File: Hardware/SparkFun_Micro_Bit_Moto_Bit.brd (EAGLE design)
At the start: 76.2 x 58.4 mm, 38 parts, among them J1 5.5x2.1mm Barrel, J2 CORTEX_DEBUGPTH, U1 CY8C4245LQI-483, U2 TPS62172, U3 micro:bit, U4 DRV8835

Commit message: Changed name from motobit to follow naming conventions
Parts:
- added D1: RED, SparkFun-LED:LED-0603
- added R3, R4: 4.7k, SparkFun-Resistors:0603
- added R5: 470, SparkFun-Resistors:0603
- U$1: device SparkFun-Hardware:STAND-OFF -> SparkFun-Aesthetics:PRODUCTION_INSTRUCTIONS
- moved U$1 82.9 mm to (-7.62, -33.0)
- moved LOGO2 14.2 mm to (15.2, 12.7)
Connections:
- new net N$6: R3.1, U1.18
- new net N$7: R4.1, U1.19
- new net N$8: D1.A, R5.2
- new net SLED: R5.1, U1.14
- net 3.3V: now also R3.2, R4.2
- net GND: now also D1.C
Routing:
- net P3.3: track 13.5 -> 18.8 mm, vias 0 -> 1
- net 3.3V: track 197.0 -> 201.8 mm, vias 1 -> 2
- net N$6: track 0.00 -> 3.71 mm
- net SLED: track 0.00 -> 3.51 mm
- net N$7: track 0.00 -> 3.28 mm
- net N$8: track 0.00 -> 1.55 mm
- net P3.2: track 14.9 -> 14.0 mm, vias 0 -> 1
- net GND: vias 27 -> 28
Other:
- board text added: "- Solder mask color : Black"
- board text added: "STAT"
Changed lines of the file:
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@@
 <layer number="37" name="tTest" color="7" fill="1" visible="no" active="yes"/>
 <layer number="38" name="bTest" color="7" fill="1" visible="no" active="yes"/>
-<layer number="39" name="tKeepout" color="4" fill="11" visible="no" active="yes"/>
-<layer number="40" name="bKeepout" color="1" fill="11" visible="no" active="yes"/>
+<layer number="39" name="tKeepout" color="4" fill="11" visible="yes" active="yes"/>
+<layer number="40" name="bKeepout" color="1" fill="11" visible="yes" active="yes"/>
 <layer number="41" name="tRestrict" color="4" fill="10" visible="no" active="yes"/>
 <layer number="42" name="bRestrict" color="1" fill="10" visible="no" active="yes"/>
@@
 <layer number="45" name="Holes" color="7" fill="1" visible="no" active="yes"/>
 <layer number="46" name="Milling" color="3" fill="1" visible="no" active="yes"/>
-<layer number="47" name="Measures" color="7" fill="1" visible="yes" active="yes"/>
+<layer number="47" name="Measures" color="7" fill="1" visible="no" active="yes"/>
 <layer number="48" name="Document" color="7" fill="1" visible="no" active="yes"/>
 <layer number="49" name="Reference" color="7" fill="1" visible="no" active="yes"/>
@@
 <text x="39.37" y="3.81" size="1.27" layer="22" font="vector" ratio="15" rot="MR180" align="bottom-center">0x59</text>
 <text x="62.23" y="0.508" size="1.27" layer="16" font="vector" ratio="15" rot="MR0" align="bottom-center">v01</text>
+<text x="26.67" y="27.813" size="1.016" layer="21" font="vector" ratio="15">STAT</text>
+<text x="-5.08" y="-45.72" size="1.27" layer="51" font="vector" ratio="15">- Solder mask color : Black</text>
 </plain>
 <attributes>
@@
 <attribute name="PROD_ID" value="CAP-08402" x="31.242" y="32.0167" size="1.778" layer="27" font="vector" ratio="15" rot="R90" display="off"/>
 </element>
-<element name="U$1" library="SparkFun-Hardware" package="STAND-OFF" value="" x="45.72" y="30.48"/>
 <element name="LOGO1" library="SparkFun-Aesthetics" package="SFE_LOGO_NAME_FLAME_.2" value="SFE_LOGO_NAME_FLAME.2_INCH" x="1.27" y="19.05"/>
-<element name="LOGO2" library="SparkFun-Aesthetics" package="OSHW-LOGO-M" value="OSHW-LOGOM" x="27.94" y="19.05"/>
+<element name="LOGO2" library="SparkFun-Aesthetics" package="OSHW-LOGO-M" value="OSHW-LOGOM" x="15.24" y="12.7"/>
 <element name="FD1" library="SparkFun-Aesthetics" package="FIDUCIAL-MICRO" value="FIDUCIALUFIDUCIAL" x="58.039" y="1.397"/>
 <element name="FD2" library="SparkFun-Aesthetics" package="FIDUCIAL-MICRO" value="FIDUCIALUFIDUCIAL" x="1.27" y="57.15"/>
@@
 <element name="TP3" library="SparkFun-Connectors" package="PAD.03X.03" value="" x="26.67" y="19.05" rot="MR0"/>
 <element name="TP4" library="SparkFun-Connectors" package="PAD.03X.03" value="" x="24.13" y="19.05" rot="MR0"/>
+<element name="R3" library="SparkFun-Resistors" package="0603" value="4.7k" x="28.448" y="23.495" rot="R180">
+<attribute name="PROD_ID" value="RES-07857" x="28.448" y="23.495" size="1.778" layer="27" ratio="15" rot="R180" display="off"/>
+</element>
+<element name="R4" library="SparkFun-Resistors" package="0603" value="4.7k" x="28.448" y="21.971" rot="R180">
+<attribute name="PROD_ID" value="RES-07857" x="28.448" y="21.971" size="1.778" layer="27" ratio="15" rot="R180" display="off"/>
+</element>
+<element name="D1" library="SparkFun-LED" package="LED-0603" value="RED" x="28.448" y="26.543">
+<attribute name="PROD_ID" value="DIO-00819" x="28.448" y="26.543" size="1.778" layer="27" ratio="15" display="off"/>
+</element>
+<element name="R5" library="SparkFun-Resistors" package="0603" value="470" x="28.448" y="25.019" rot="R180">
+<attribute name="PROD_ID" value="RES-07869" x="28.448" y="25.019" size="1.778" layer="27" ratio="15" rot="R180" display="off"/>
+</element>
+<element name="U$1" library="SparkFun-Aesthetics" package="PRODUCTION_INSTRUCTIONS" value="" x="-7.62" y="-33.02"/>
 </elements>
 <signals>
@@
 <wire x1="33.5814" y1="27.051" x2="33.02" y2="27.051" width="0.2032" layer="1"/>
 <contactref element="TP4" pad="P$1"/>
+<via x="45.72" y="30.48" extent="1-16" drill="3.302"/>
+<contactref element="D1" pad="C"/>
 </signal>
 <signal name="3.3V">
@@
 <wire x1="26.67" y1="16.637" x2="29.21" y2="14.097" width="0.6096" layer="16"/>
 <wire x1="29.21" y1="14.097" x2="30.226" y2="14.097" width="0.6096" layer="16"/>
+<contactref element="R4" pad="2"/>
+<contactref element="R3" pad="2"/>
+<wire x1="26.67" y1="19.05" x2="26.67" y2="19.392" width="0.6096" layer="16"/>
+<wire x1="26.67" y1="19.392" x2="27.598" y2="20.32" width="0.6096" layer="16"/>
+<via x="27.598" y="20.32" extent="1-16" drill="0.381"/>
+<wire x1="27.598" y1="20.32" x2="27.598" y2="21.971" width="0.6096" layer="1"/>
+<wire x1="27.598" y1="21.971" x2="27.598" y2="23.495" width="0.6096" layer="1"/>
 </signal>
 <signal name="SDA">
@@
 <contactref element="U1" pad="12"/>
 <contactref element="J2" pad="2"/>
-<wire x1="30.226" y1="15.367" x2="30.226" y2="17.907" width="0.2032" layer="1"/>
-<wire x1="30.226" y1="17.907" x2="30.861" y2="18.542" width="0.2032" layer="1"/>
-<wire x1="30.861" y1="18.542" x2="30.861" y2="24.067996875" width="0.2032" layer="1"/>
-<wire x1="30.861" y1="24.067996875" x2="31.657003125" y2="24.864" width="0.2032" layer="1"/>
-<wire x1="31.657003125" y1="24.864" x2="32.3314" y2="24.864" width="0.2032" layer="1"/>
 <contactref element="TP1" pad="P$1"/>
-<wire x1="29.21" y1="19.05" x2="30.226" y2="18.034" width="0.254" layer="16"/>
-<wire x1="30.226" y1="18.034" x2="30.226" y2="15.367" width="0.254" layer="16"/>
+<wire x1="32.3314" y1="24.864" x2="31.823384375" y2="24.864" width="0.254" layer="1"/>
+<wire x1="31.823384375" y1="24.864" x2="31.623" y2="25.064384375" width="0.254" layer="1"/>
+<wire x1="31.623" y1="25.064384375" x2="31.623" y2="26.035" width="0.254" layer="1"/>
+<via x="31.623" y="26.035" extent="1-16" drill="0.381"/>
+<wire x1="30.226" y1="15.367" x2="30.226" y2="19.05" width="0.254" layer="16"/>
+<wire x1="30.226" y1="19.05" x2="30.226" y2="24.638" width="0.254" layer="16"/>
+<wire x1="30.226" y1="24.638" x2="31.623" y2="26.035" width="0.254" layer="16"/>
+<wire x1="29.21" y1="19.05" x2="30.226" y2="19.05" width="0.254" layer="16"/>
 </signal>
 <signal name="P3.3">
 <contactref element="U1" pad="13"/>
 <contactref element="J2" pad="4"/>
-<wire x1="31.496" y1="15.367" x2="31.496" y2="17.907" width="0.2032" layer="1"/>
-<wire x1="31.496" y1="17.907" x2="31.369" y2="18.034" width="0.2032" layer="1"/>
-<wire x1="31.369" y1="18.034" x2="31.369" y2="23.91688125" width="0.2032" layer="1"/>
-<wire x1="31.369" y1="23.91688125" x2="31.81611875" y2="24.364" width="0.2032" layer="1"/>
-<wire x1="31.81611875" y1="24.364" x2="32.3314" y2="24.364" width="0.2032" layer="1"/>
 <contactref element="TP2" pad="P$1"/>
-<wire x1="31.75" y1="19.05" x2="31.496" y2="18.796" width="0.254" layer="16"/>
-<wire x1="31.496" y1="18.796" x2="31.496" y2="15.367" width="0.254" layer="16"/>
+<wire x1="32.3314" y1="24.364" x2="31.466696875" y2="24.364" width="0.254" layer="1"/>
+<wire x1="31.466696875" y1="24.364" x2="30.734" y2="25.096696875" width="0.254" layer="1"/>
+<wire x1="30.734" y1="25.096696875" x2="30.734" y2="26.797" width="0.254" layer="1"/>
+<via x="31.242" y="27.305" extent="1-16" drill="0.381"/>
+<wire x1="30.734" y1="26.797" x2="31.242" y2="27.305" width="0.254" layer="1"/>
+<wire x1="31.75" y1="19.05" x2="30.861" y2="19.05" width="0.254" layer="16"/>
+<wire x1="30.861" y1="19.05" x2="30.861" y2="24.13" width="0.254" layer="16"/>
+<wire x1="30.861" y1="24.13" x2="32.385" y2="25.654" width="0.254" layer="16"/>
+<wire x1="32.385" y1="25.654" x2="32.385" y2="26.67" width="0.254" layer="16"/>
+<wire x1="32.385" y1="26.67" x2="31.75" y2="27.305" width="0.254" layer="16"/>
+<wire x1="31.75" y1="27.305" x2="31.242" y2="27.305" width="0.254" layer="16"/>
+<wire x1="31.496" y1="15.367" x2="30.861" y2="16.002" width="0.254" layer="16"/>
+<wire x1="30.861" y1="16.002" x2="30.861" y2="19.05" width="0.254" layer="16"/>
 </signal>
 <signal name="P0.4">
@@
 <wire x1="34.5814" y1="19.30425" x2="34.5814" y2="20.114" width="0.254" layer="1"/>
 </signal>
+<signal name="N$6">
+<contactref element="U1" pad="18"/>
+<contactref element="R3" pad="1"/>
+<wire x1="29.298" y1="23.495" x2="30.033740625" y2="23.495" width="0.254" layer="1"/>
+<wire x1="31.664740625" y1="21.864" x2="32.3314" y2="21.864" width="0.254" layer="1"/>
+<wire x1="31.664740625" y1="21.864" x2="30.033740625" y2="23.495" width="0.254" layer="1"/>
+</signal>
+<signal name="N$7">
+<contactref element="U1" pad="19"/>
+<contactref element="R4" pad="1"/>
+<wire x1="29.298" y1="21.971" x2="30.127" y2="21.971" width="0.254" layer="1"/>
+<wire x1="30.734" y1="21.364" x2="32.3314" y2="21.364" width="0.254" layer="1"/>
+<wire x1="30.734" y1="21.364" x2="30.127" y2="21.971" width="0.254" layer="1"/>
+</signal>
+<signal name="SLED">
+<contactref element="U1" pad="14"/>
+<contactref element="R5" pad="1"/>
+<wire x1="29.298" y1="25.019" x2="30.0134625" y2="25.019" width="0.254" layer="1"/>
+<wire x1="31.1684625" y1="23.864" x2="32.3314" y2="23.864" width="0.254" layer="1"/>
+<wire x1="31.1684625" y1="23.864" x2="30.0134625" y2="25.019" width="0.254" layer="1"/>
+</signal>
+<signal name="N$8">
+<contactref element="R5" pad="2"/>
+<contactref element="D1" pad="A"/>
+<wire x1="27.571" y1="26.543" x2="27.571" y2="25.019" width="0.254" layer="1"/>
+<wire x1="27.571" y1="25.019" x2="27.598" y2="25.019" width="0.254" layer="1"/>
+</signal>
 </signals>

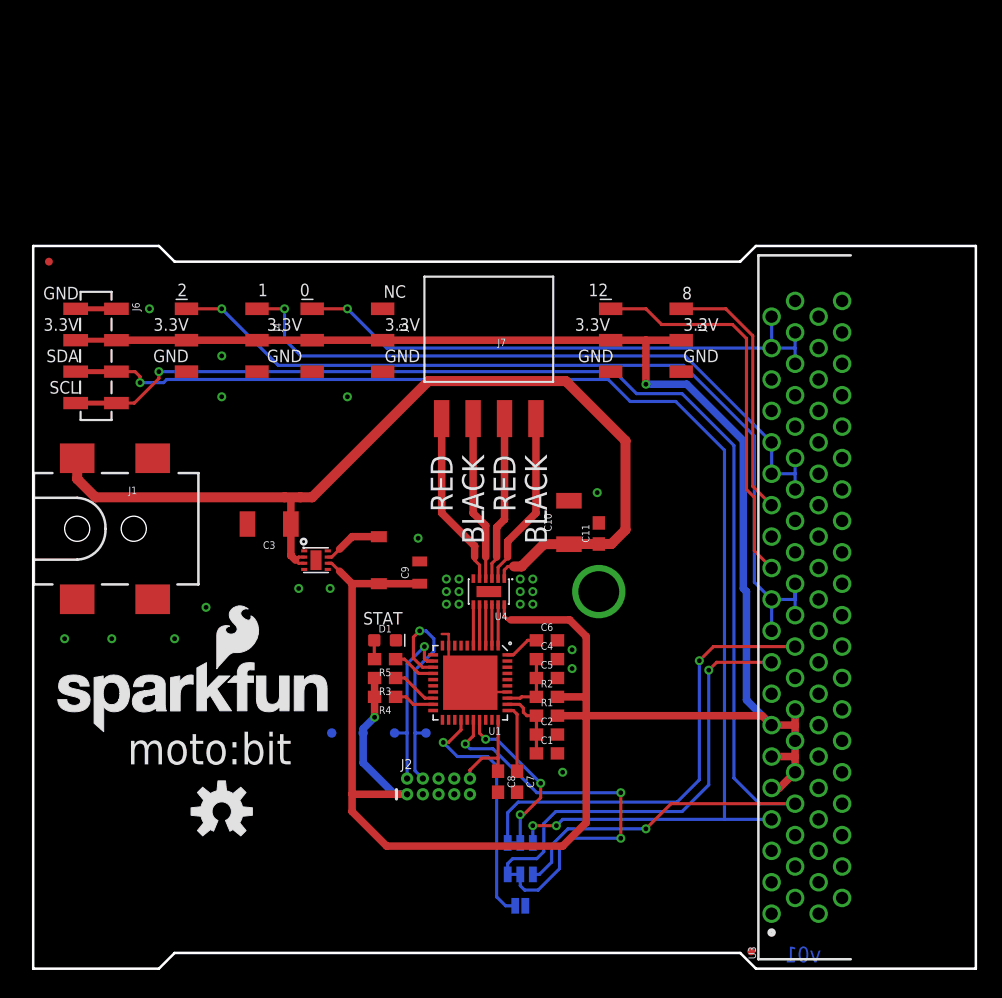
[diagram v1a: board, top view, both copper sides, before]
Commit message: Design Review Changes
- Added staking vias to barrel connector and motor connector
- Added two servo connectors
- Moved vias that were exposed for motor driver heatsink
- Added selective solder path
- Added mounting holes
- Rounded corners to match micro:bit
- Rotated silk to match micro:bit silk orientation
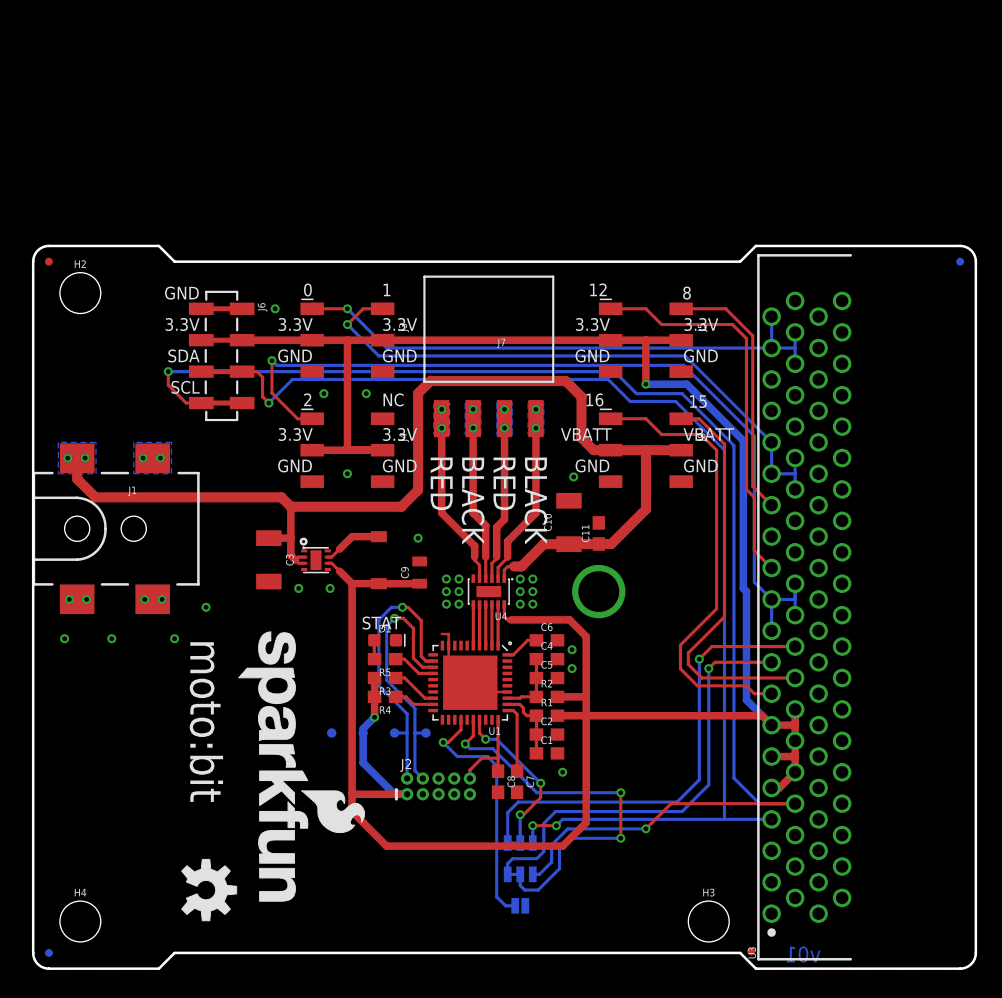
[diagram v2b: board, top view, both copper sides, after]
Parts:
- added FD3, FD4: FIDUCIALUFIDUCIAL, SparkFun-Aesthetics:FIDUCIAL-MICRO
- added H2, H3, H4: STAND-OFF, SparkFun-Hardware:STAND-OFF
- added J8: (no value), SparkFun-Connectors:2X3_SMD
- J6: value (none) -> 1X04_SMD_STRAIGHT_COMBO
- L1: value 4.7µH -> 2.2µH
- moved LOGO1 17.6 mm to (16.5, 27.9), turned to 270 degrees
- moved J4 13.5 mm to (25.4, 41.9)
- moved J6 10.2 mm to (15.2, 53.3)
- moved LOGO2 6.48 mm to (14.0, 6.35), turned to 270 degrees
- moved C3 2.90 mm to (19.1, 33.0), turned to 270 degrees
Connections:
- removed net BIN1: U3.A16
- removed net BIN2: U3.A15
- new net SERVO_15: J8.2, U3.A16
- new net SERVO_16: J8.1, U3.A15
- net ANALOG_1: now also J3.2; no longer J4.2
- net GND: now also J8.5, J8.6
- net V_BATT: now also J8.3, J8.4
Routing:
- net SERVO_16: track 0.00 -> 36.7 mm
- net SERVO_15: track 0.00 -> 32.5 mm
- net V_BATT: track 79.7 -> 93.4 mm, vias 0 -> 2
- net P3.2: track 14.0 -> 23.1 mm
- net SDA: track 106.3 -> 98.2 mm
- net 3.3V: track 201.8 -> 209.1 mm
- net ANALOG_1: track 54.5 -> 48.6 mm
- net P3.3: track 18.8 -> 21.5 mm
- net SCL: track 110.8 -> 112.9 mm
- net ANALOG_2: track 72.2 -> 70.3 mm
- net N$5: track 0.00 -> 1.40 mm, vias 0 -> 2
- net BO2: track 14.2 -> 14.9 mm, vias 0 -> 2
- net BO1: track 13.4 -> 14.1 mm, vias 0 -> 2
- net AO2: track 13.4 -> 14.1 mm, vias 0 -> 2
- net AO1: track 14.2 -> 14.9 mm, vias 0 -> 2
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- added copper zone on layer 16, net AO1
- added copper zone on layer 16, net AO2
- added copper zone on layer 16, net BO1
- added copper zone on layer 16, net BO2
- added copper zone on layer 16, net N$5
- added copper zone on layer 16, net V_BATT
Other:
- outline, holes or cut-outs redrawn
- board text added: "15"
- board text added: "16"
- board text added: "VBATT"

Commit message: QC Fixes
- Removed excess copper around PSoC center pad
- Added names and values to buck converter and inductor
- Added note about solder mask color finish
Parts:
- L1: value 2.2µH -> 2.2µH/±20%/1.5A
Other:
- board text added: "- Solder mask color : Black (Gloss if available)"
- board text removed: "- Solder mask color : Black"
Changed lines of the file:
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@@
 <layer number="20" name="Dimension" color="15" fill="1" visible="yes" active="yes"/>
 <layer number="21" name="tPlace" color="16" fill="1" visible="yes" active="yes"/>
-<layer number="22" name="bPlace" color="14" fill="1" visible="no" active="yes"/>
+<layer number="22" name="bPlace" color="14" fill="1" visible="yes" active="yes"/>
 <layer number="23" name="tOrigins" color="15" fill="1" visible="yes" active="yes"/>
-<layer number="24" name="bOrigins" color="15" fill="1" visible="no" active="yes"/>
+<layer number="24" name="bOrigins" color="15" fill="1" visible="yes" active="yes"/>
 <layer number="25" name="tNames" color="7" fill="1" visible="no" active="yes"/>
 <layer number="26" name="bNames" color="7" fill="1" visible="no" active="yes"/>
 <layer number="27" name="tValues" color="7" fill="1" visible="no" active="yes"/>
 <layer number="28" name="bValues" color="7" fill="1" visible="no" active="yes"/>
-<layer number="29" name="tStop" color="7" fill="3" visible="no" active="yes"/>
-<layer number="30" name="bStop" color="7" fill="6" visible="no" active="yes"/>
+<layer number="29" name="tStop" color="7" fill="3" visible="yes" active="yes"/>
+<layer number="30" name="bStop" color="7" fill="6" visible="yes" active="yes"/>
 <layer number="31" name="tCream" color="7" fill="4" visible="no" active="yes"/>
 <layer number="32" name="bCream" color="7" fill="5" visible="no" active="yes"/>
@@
 <layer number="38" name="bTest" color="7" fill="1" visible="no" active="yes"/>
 <layer number="39" name="tKeepout" color="4" fill="11" visible="yes" active="yes"/>
-<layer number="40" name="bKeepout" color="1" fill="11" visible="yes" active="yes"/>
+<layer number="40" name="bKeepout" color="1" fill="11" visible="no" active="yes"/>
 <layer number="41" name="tRestrict" color="4" fill="10" visible="no" active="yes"/>
 <layer number="42" name="bRestrict" color="1" fill="10" visible="no" active="yes"/>
 <layer number="43" name="vRestrict" color="2" fill="10" visible="no" active="yes"/>
 <layer number="44" name="Drills" color="7" fill="1" visible="no" active="yes"/>
-<layer number="45" name="Holes" color="7" fill="1" visible="no" active="yes"/>
+<layer number="45" name="Holes" color="7" fill="1" visible="yes" active="yes"/>
 <layer number="46" name="Milling" color="3" fill="1" visible="no" active="yes"/>
 <layer number="47" name="Measures" color="7" fill="1" visible="yes" active="yes"/>
@@
 <text x="62.23" y="0.508" size="1.27" layer="16" font="vector" ratio="15" rot="MR0" align="bottom-center">v01</text>
 <text x="26.543" y="27.432" size="1.016" layer="21" font="vector" ratio="15">STAT</text>
-<text x="-5.08" y="-45.72" size="1.27" layer="51" font="vector" ratio="15">- Solder mask color : Black</text>
+<text x="-5.08" y="-45.72" size="1.27" layer="51" font="vector" ratio="15">- Solder mask color : Black (Gloss if available)</text>
 <text x="44.704" y="42.672" size="1.016" layer="21" font="vector" ratio="15" align="bottom-center">VBATT</text>
 <text x="54.61" y="42.672" size="1.016" layer="21" font="vector" ratio="15" align="bottom-center">VBATT</text>
@@
 <wire x1="62.23" y1="53.34" x2="62.23" y2="3.81" width="8.9916" layer="48"/>
 <wire x1="62.23" y1="3.81" x2="67.31" y2="-1.27" width="8.9916" layer="48"/>
+<wire x1="33.02" y1="22.733" x2="33.02" y2="23.495" width="0.254" layer="41"/>
+<wire x1="34.925" y1="20.7899" x2="35.687" y2="20.7899" width="0.254" layer="41"/>
 </plain>
 <attributes>
@@
 <attribute name="PROD_ID" value="IC-11307" x="22.86" y="33.02" size="1.778" layer="27" font="vector" ratio="15" rot="R270" display="off"/>
 </element>
-<element name="L1" library="SparkFun-Coils" package="INDUCTOR_2.2UH" value="2.2µH" x="27.94" y="33.02" rot="R270">
+<element name="L1" library="SparkFun-Coils" package="INDUCTOR_2.2UH" value="2.2µH/±20%/1.5A" x="27.94" y="33.02" rot="R270">
 <attribute name="PROD_ID" value="NDUC-09513" x="27.94" y="33.02" size="1.778" layer="27" font="vector" ratio="15" rot="R270" display="off"/>
 </element>
